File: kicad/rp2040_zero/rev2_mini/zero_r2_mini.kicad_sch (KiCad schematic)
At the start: 6 parts, among them J3 Debug port, J5 Debug port, Q1 DMG2302U, U1 RP2040-Zero

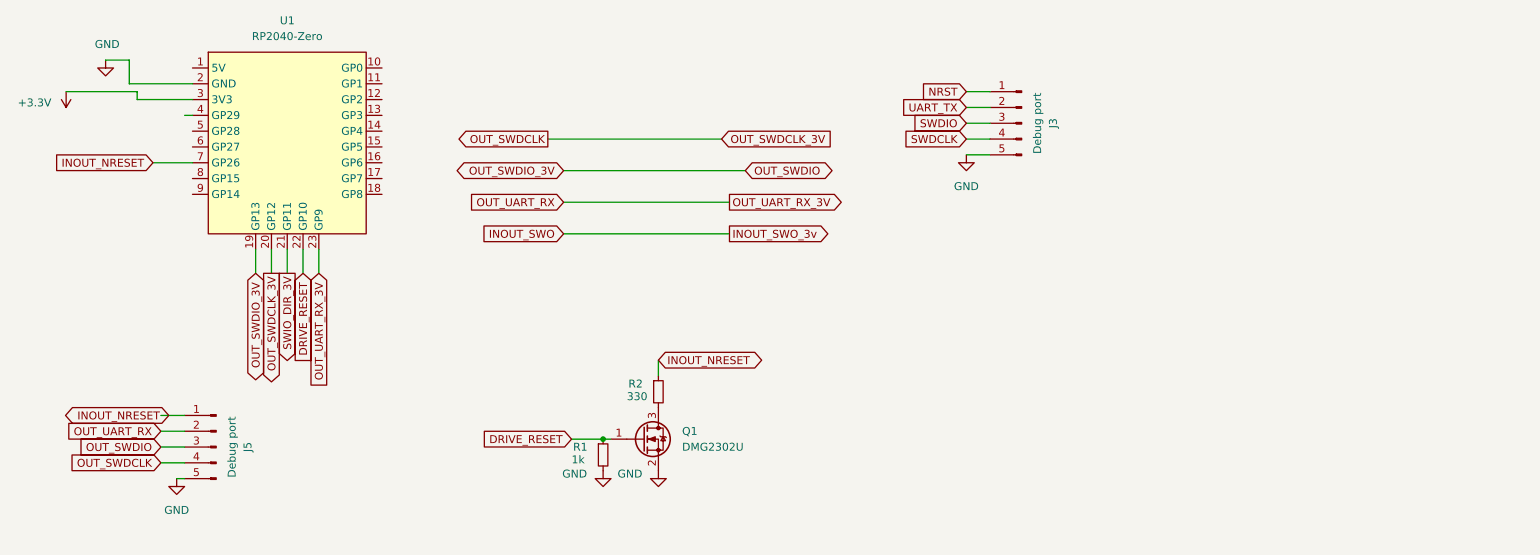
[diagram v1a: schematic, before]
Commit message: kicad: add pullup resistor on rp2040
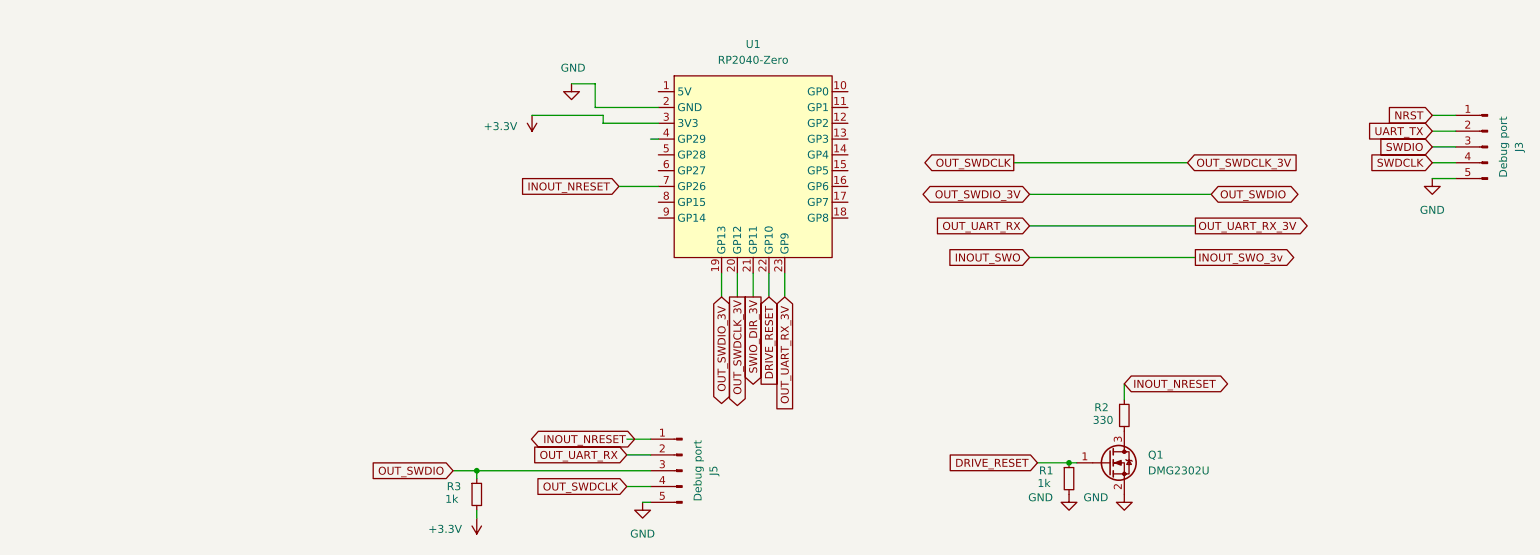
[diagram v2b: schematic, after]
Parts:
- added R3: 1k, Resistor_SMD:R_0603_1608Metric, symbol Device:R_Small
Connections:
- net +3.3V: now also R3.2
- net OUT_SWDIO: now also R3.1
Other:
- moved on the sheet: J3, J5, Q1, R1, R2, U1
